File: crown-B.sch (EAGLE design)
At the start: 15 parts

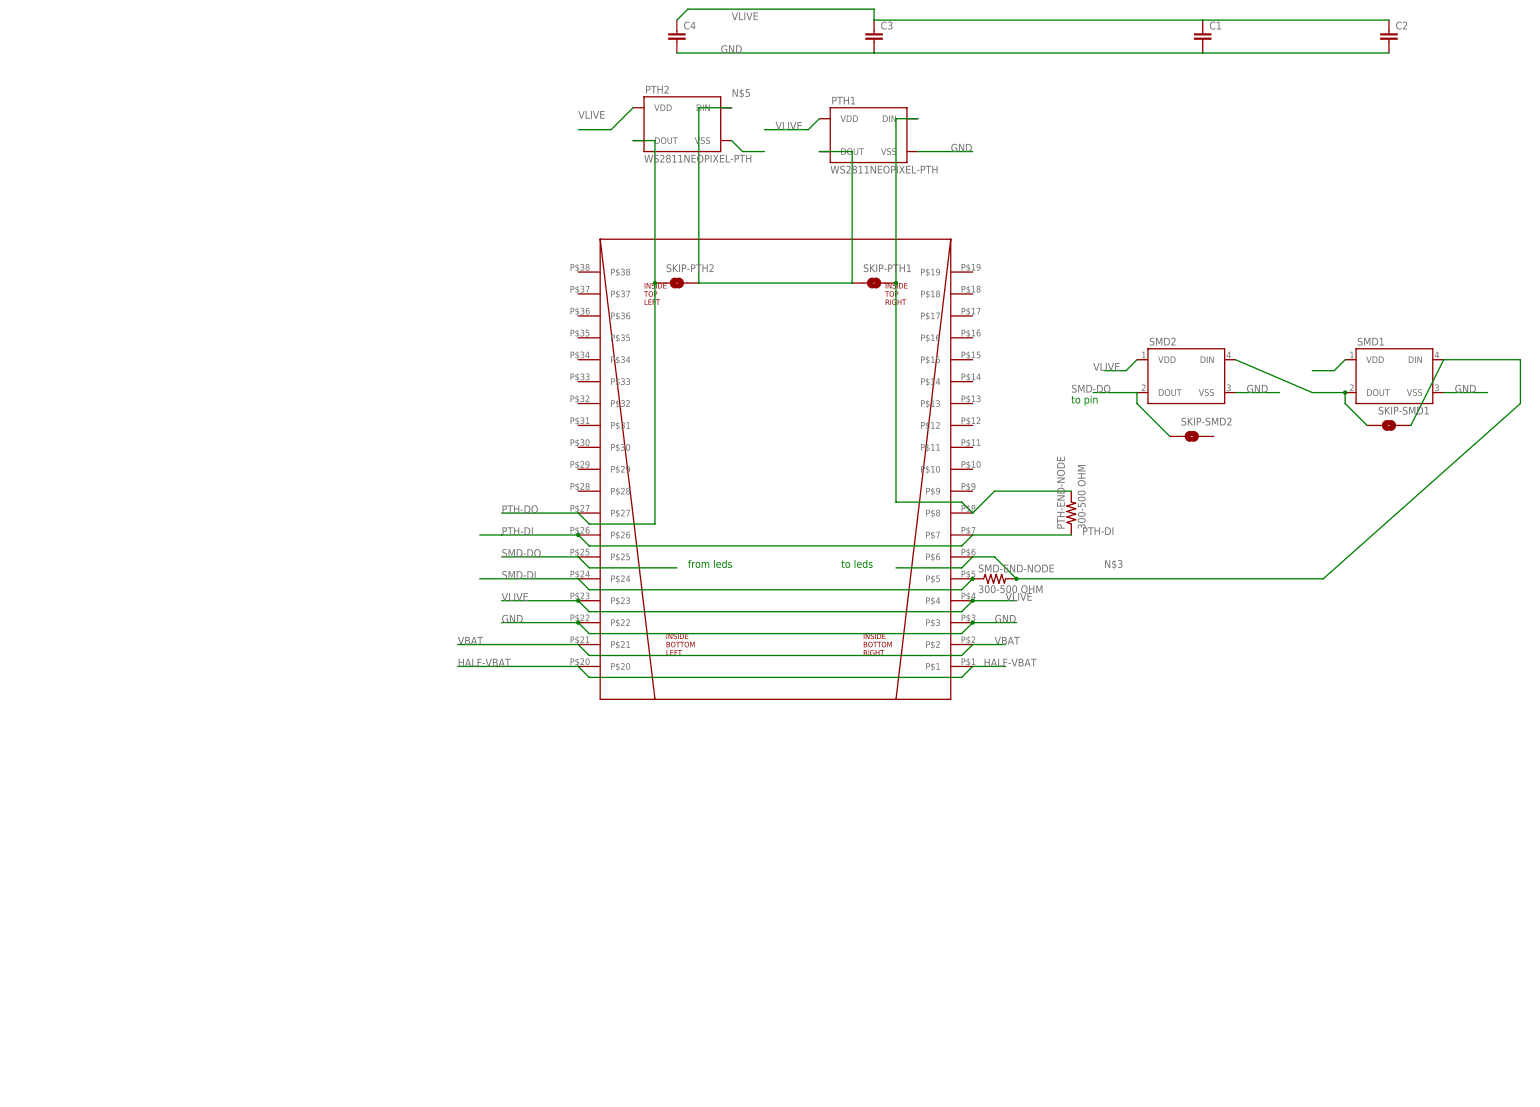
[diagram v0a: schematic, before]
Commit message: Added B plate, which holds battery (best for lipo)
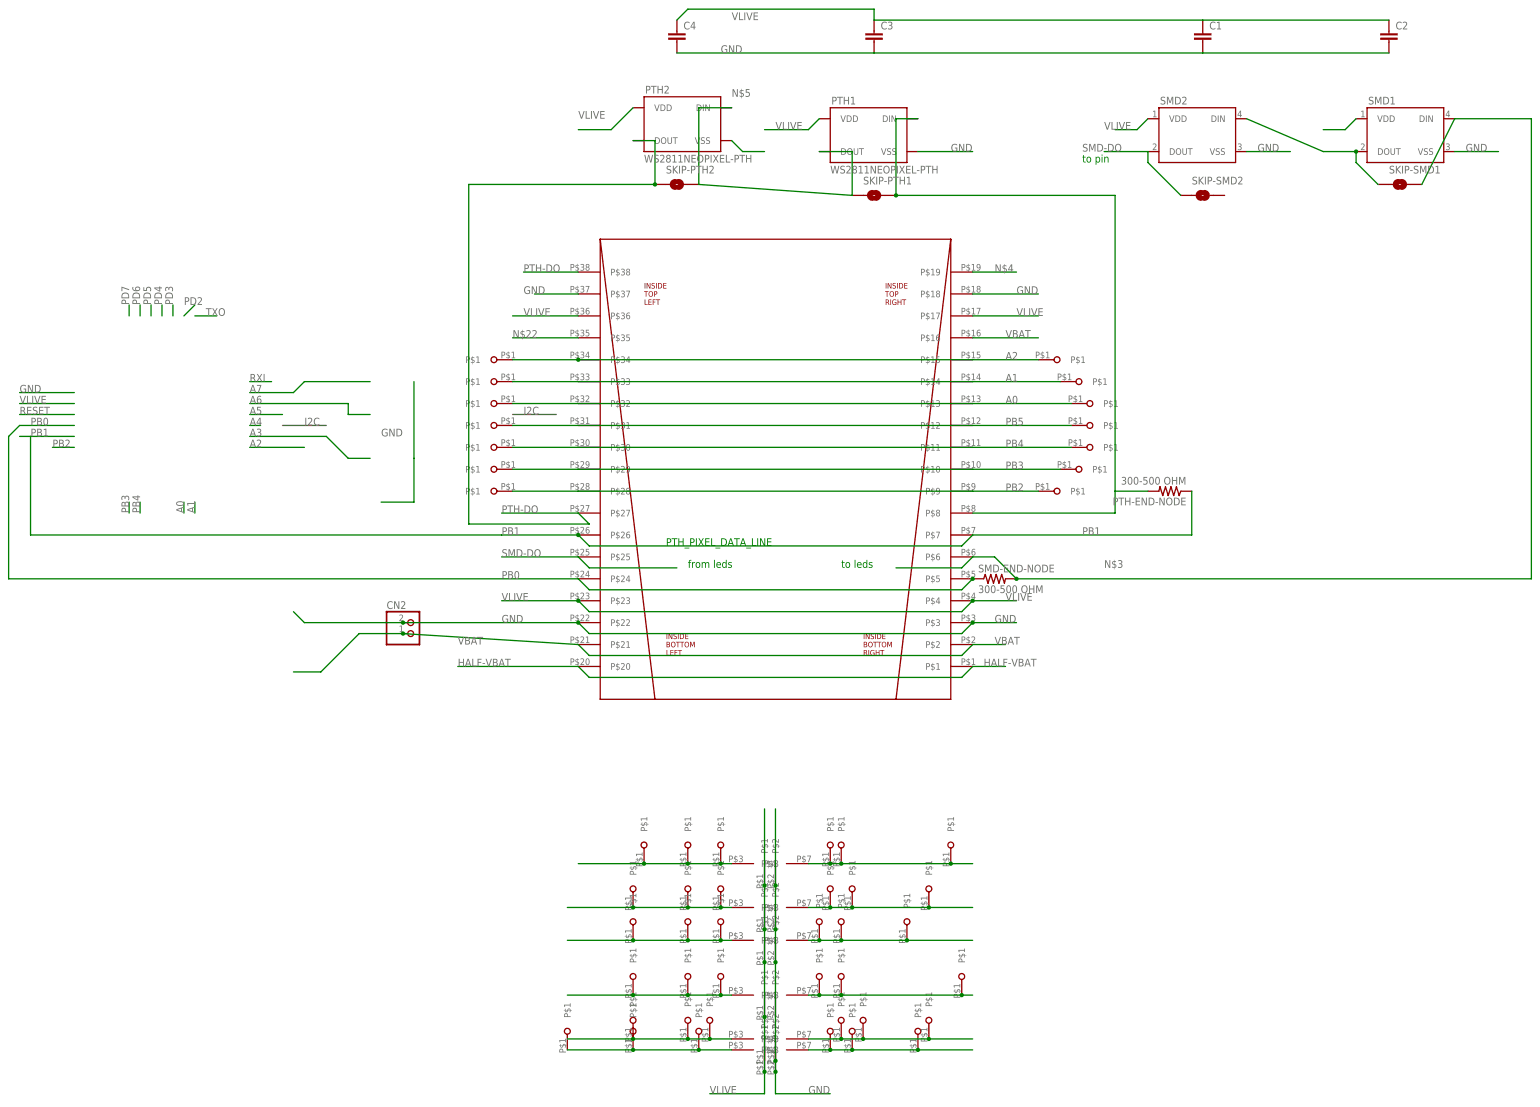
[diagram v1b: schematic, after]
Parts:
- added CN2: (no value), adafruit:JST_2PIN-SMT-RA
- added U$1, U$3, U$4, U$5, U$6, U$7: SMD_BREADBOARD, pcb_crown:SMD_BREADBOARD
- added U$10, U$11, U$12, U$13, U$14, U$15, U$16, U$17, U$22, U$23, U$24, U$25, U$26, U$27, U$28, U$29, U$34, U$35, U$36, U$37, U$38, U$39, U$40, U$41, U$42, U$43, U$44, U$45, U$46, U$47, U$48, U$49, U$50, U$51, U$52, U$53, U$54, U$55, U$56, U$57, U$58, U$59, U$62, U$63, U$64, U$65, U$68, U$69, U$70, U$71: SMD_PAD, pcb_crown:SMD_PAD
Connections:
- net PTH-DI renamed PB1
- net SMD-DI renamed PB0
- new net A0: U$2.P$13, U$2.P$32, U$44.P$1, U$55.P$1
- new net A1: U$2.P$14, U$2.P$33, U$43.P$1, U$56.P$1
- new net A2: U$2.P$15, U$2.P$34, U$42.P$1, U$58.P$1
- new net N$11: U$14.P$1, U$15.P$1, U$5.P$3, U$57.P$1
- new net N$12: U$12.P$1, U$13.P$1, U$50.P$1, U$6.P$3
- new net N$13: U$10.P$1, U$11.P$1, U$49.P$1, U$7.P$3
- new net N$14: U$40.P$1, U$41.P$1, U$7.P$4, U$71.P$1
- new net N$15: U$38.P$1, U$39.P$1, U$6.P$4, U$70.P$1
- new net N$16: U$36.P$1, U$37.P$1, U$5.P$4, U$69.P$1
- new net N$17: U$34.P$1, U$35.P$1, U$4.P$4, U$68.P$1
- new net N$2: U$1.P$3, U$24.P$1, U$25.P$1, U$63.P$1
- new net N$20: U$28.P$1, U$29.P$1, U$3.P$4, U$65.P$1
- new net N$21: U$1.P$4, U$26.P$1, U$27.P$1, U$64.P$1
- new net N$22: U$2.P$35
- new net N$6: U$22.P$1, U$23.P$1, U$3.P$3, U$62.P$1
- new net N$9: U$16.P$1, U$17.P$1, U$4.P$3, U$59.P$1
- new net PB2: U$2.P$28, U$2.P$9, U$48.P$1, U$51.P$1
- new net PB3: U$2.P$10, U$2.P$29, U$47.P$1, U$52.P$1
- new net PB4: U$2.P$11, U$2.P$30, U$46.P$1, U$53.P$1
- new net PB5: U$2.P$12, U$2.P$31, U$45.P$1, U$54.P$1
- net GND: now also CN2.1, U$1.P$2, U$2.P$18, U$2.P$37, U$3.P$2, U$4.P$2, U$5.P$2, U$6.P$2, U$7.P$2
- net N$4: now also U$2.P$19
- net PTH-DO: now also U$2.P$38
- net VBAT: now also CN2.2, U$2.P$16
- net VLIVE: now also U$1.P$1, U$2.P$17, U$2.P$36, U$3.P$1, U$4.P$1, U$5.P$1, U$6.P$1, U$7.P$1
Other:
- note added: "PTH_PIXEL_DATA_LINE"
- moved on the sheet: PTH-END-NODE, SKIP-PTH1, SKIP-PTH2, SKIP-SMD1, SKIP-SMD2, SMD1, SMD2

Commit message: forgot a connection on skip-smd bits
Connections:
- net N$10: now also SKIP-SMD2.2
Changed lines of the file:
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@@
 <pinref part="SMD2" gate="G$1" pin="DIN"/>
 <wire x1="220.98" y1="119.38" x2="203.2" y2="127" width="0.2032" layer="91"/>
+<pinref part="SKIP-SMD2" gate="1" pin="2"/>
+<wire x1="198.12" y1="109.22" x2="198.12" y2="121.92" width="0.2032" layer="91"/>
+<wire x1="198.12" y1="121.92" x2="203.2" y2="127" width="0.2032" layer="91"/>
 </segment>
 </net>
